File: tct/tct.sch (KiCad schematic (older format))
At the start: 6 parts, among them IC1 ATTINY85-P, P1 CONN_01X02, U1 DIL40_IC

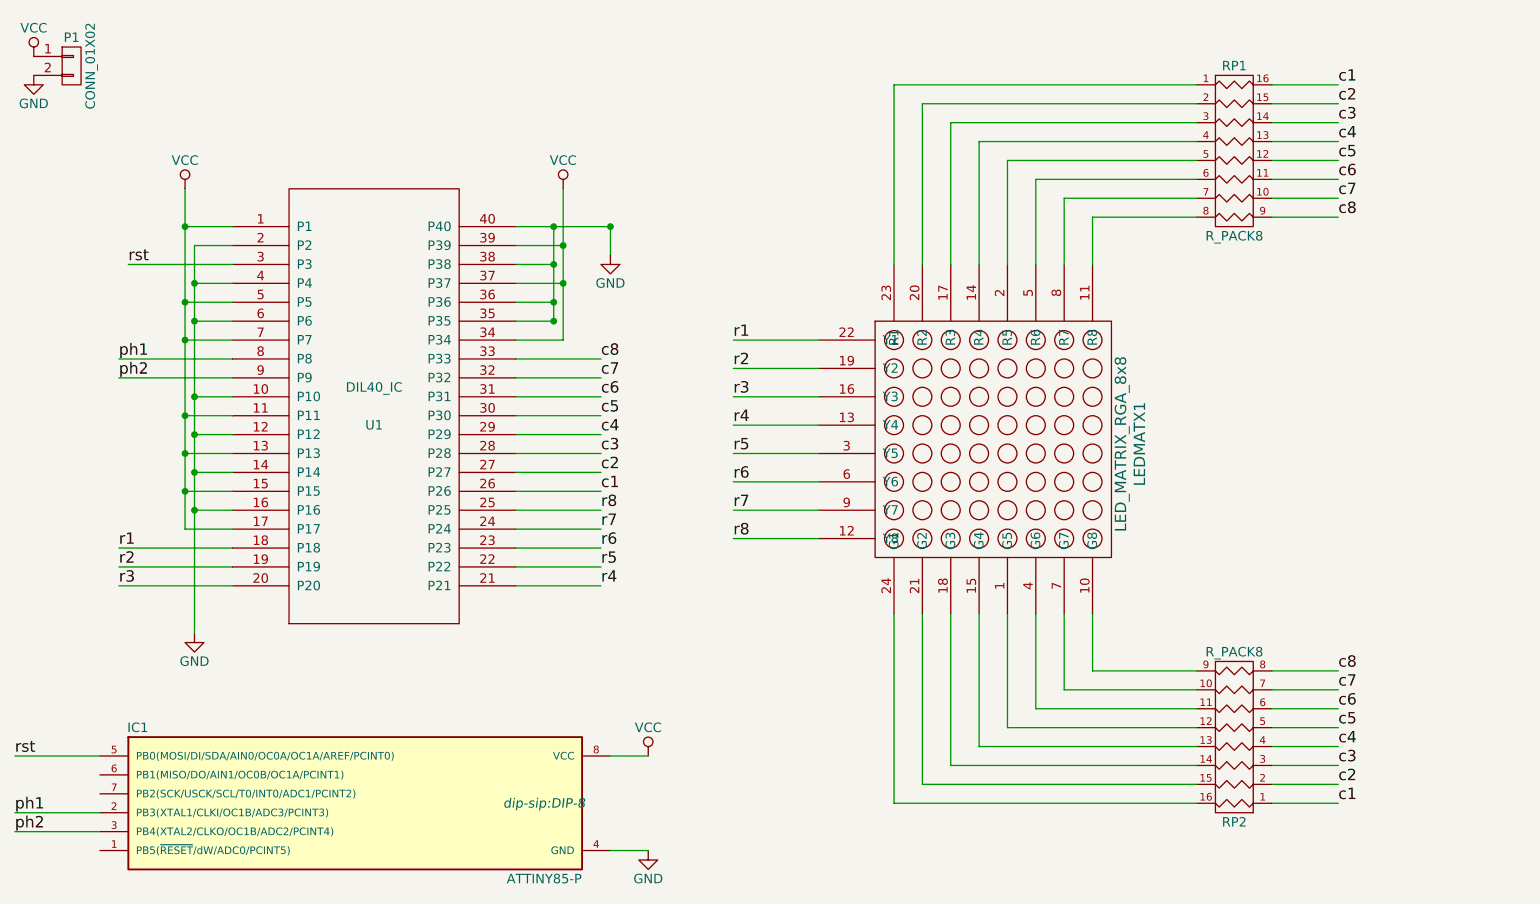
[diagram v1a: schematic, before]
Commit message: fixed layout with proper display pinout
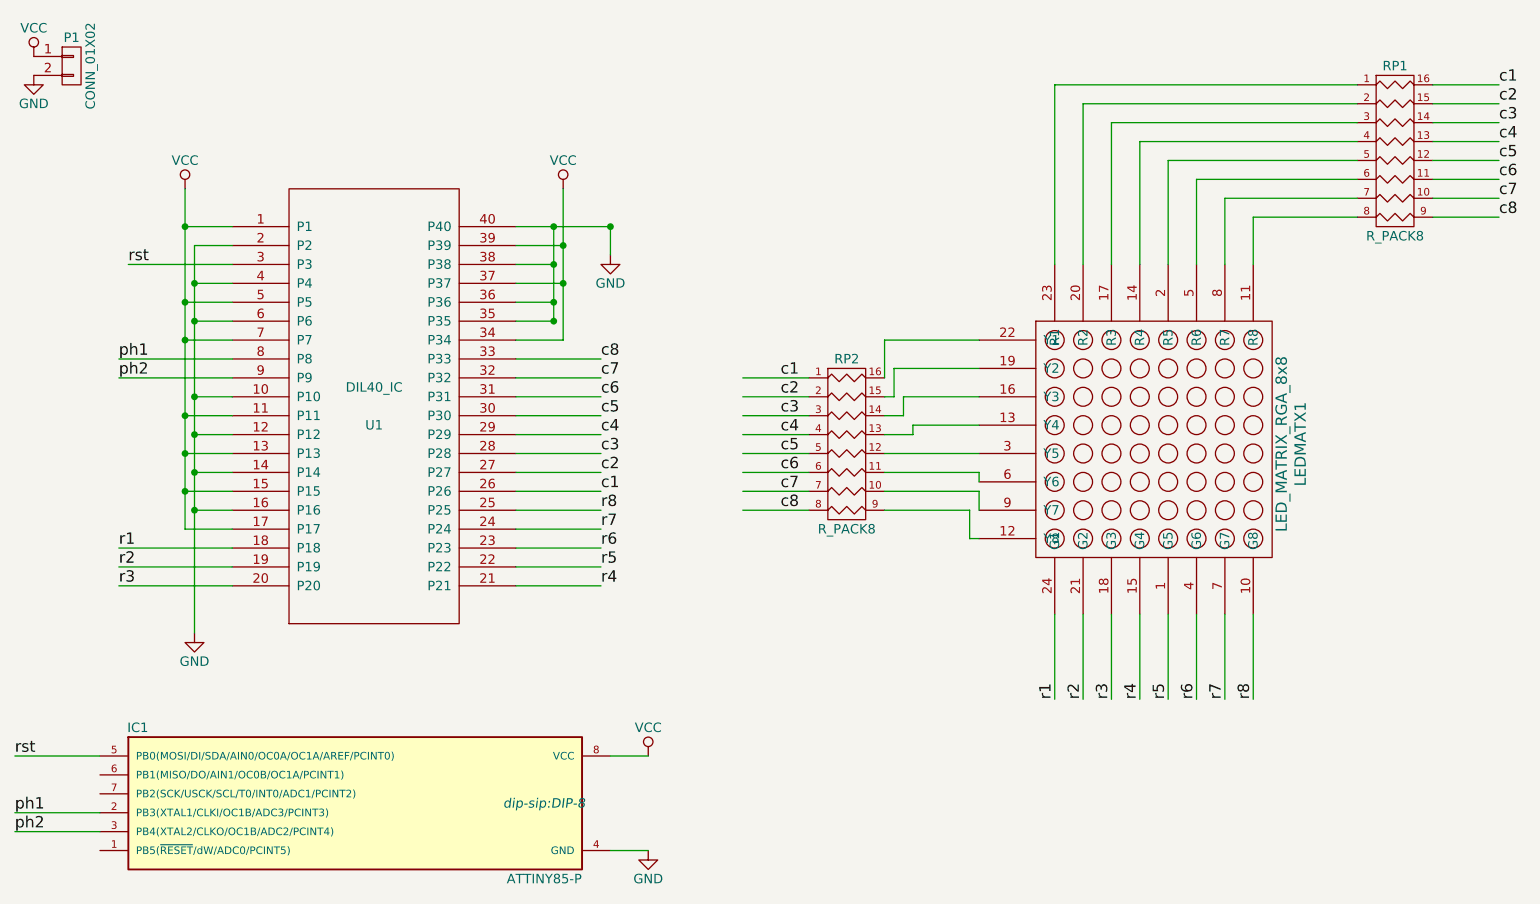
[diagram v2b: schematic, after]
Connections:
- wire segments 106 -> 109
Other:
- moved on the sheet: LEDMATX1, RP1, RP2
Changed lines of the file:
@@
 L LED_MATRIX_RGA_8x8 LEDMATX1
 U 1 1 58A54426
-P 8100 3350
-F 0 "LEDMATX1" V 8850 3350 60  0000 C CNN
-F 1 "LED_MATRIX_RGA_8x8" V 8750 3350 60  0000 C CNN
-F 2 "LED_MATRIX_RG_8x8:LED_MATRIX_RG_8x8" H 8100 3350 60  0001 C CNN
-F 3 "" H 8100 3350 60  0001 C CNN
-	1    8100 3350
+P 8950 3350
+F 0 "LEDMATX1" V 9700 3350 60  0000 C CNN
+F 1 "LED_MATRIX_RGA_8x8" V 9600 3350 60  0000 C CNN
+F 2 "LED_MATRIX_RG_8x8:LED_MATRIX_RG_8x8" H 8950 3350 60  0001 C CNN
+F 3 "" H 8950 3350 60  0001 C CNN
+	1    8950 3350
 	1    0    0    -1
 $EndComp
@@
 L R_PACK8 RP2
 U 1 1 58A5484C
-P 9350 4900
-F 0 "RP2" H 9350 5350 50  0000 C CNN
-F 1 "R_PACK8" H 9350 4450 50  0000 C CNN
-F 2 "Resistors_SMD:R_Array_Convex_8x0602" H 9350 4900 50  0001 C CNN
-F 3 "" H 9350 4900 50  0000 C CNN
-	1    9350 4900
-	-1   0    0    1
+P 7300 3350
+F 0 "RP2" H 7300 3800 50  0000 C CNN
+F 1 "R_PACK8" H 7300 2900 50  0000 C CNN
+F 2 "Resistors_SMD:R_Array_Convex_8x0602" H 7300 3350 50  0001 C CNN
+F 3 "" H 7300 3350 50  0000 C CNN
+	1    7300 3350
+	1    0    0    -1
 $EndComp
 $Comp
 L R_PACK8 RP1
 U 1 1 58A5487D
-P 9350 1800
-F 0 "RP1" H 9350 2250 50  0000 C CNN
-F 1 "R_PACK8" H 9350 1350 50  0000 C CNN
-F 2 "Resistors_SMD:R_Array_Convex_8x0602" H 9350 1800 50  0001 C CNN
-F 3 "" H 9350 1800 50  0000 C CNN
-	1    9350 1800
+P 10200 1800
+F 0 "RP1" H 10200 2250 50  0000 C CNN
+F 1 "R_PACK8" H 10200 1350 50  0000 C CNN
+F 2 "Resistors_SMD:R_Array_Convex_8x0602" H 10200 1800 50  0001 C CNN
+F 3 "" H 10200 1800 50  0000 C CNN
+	1    10200 1800
 	1    0    0    -1
 $EndComp
@@
 $EndComp
 Wire Wire Line
-	7550 5250 7550 4250
-Wire Wire Line
-	9150 5250 7550 5250
-Wire Wire Line
-	7700 5150 9150 5150
-Wire Wire Line
-	7700 4250 7700 5150
-Wire Wire Line
-	7850 5050 7850 4250
-Wire Wire Line
-	9150 5050 7850 5050
-Wire Wire Line
-	8000 4950 9150 4950
-Wire Wire Line
-	8000 4250 8000 4950
-Wire Wire Line
-	8150 4850 8150 4250
-Wire Wire Line
-	9150 4850 8150 4850
-Wire Wire Line
-	8300 4750 9150 4750
-Wire Wire Line
-	8300 4250 8300 4750
-Wire Wire Line
-	8450 4650 9150 4650
-Wire Wire Line
-	8450 4250 8450 4650
-Wire Wire Line
-	8600 4550 9150 4550
-Wire Wire Line
-	8600 4250 8600 4550
-Wire Wire Line
-	8600 2400 8600 2150
-Wire Wire Line
-	8600 2150 9150 2150
-Wire Wire Line
-	9150 2050 8450 2050
-Wire Wire Line
-	8450 2050 8450 2400
-Wire Wire Line
-	8300 2400 8300 1950
-Wire Wire Line
-	8300 1950 9150 1950
-Wire Wire Line
-	9150 1850 8150 1850
-Wire Wire Line
-	8150 1850 8150 2400
-Wire Wire Line
-	8000 2400 8000 1750
-Wire Wire Line
-	8000 1750 9150 1750
-Wire Wire Line
-	9150 1650 7850 1650
-Wire Wire Line
-	7850 1650 7850 2400
-Wire Wire Line
-	7700 2400 7700 1550
-Wire Wire Line
-	7700 1550 9150 1550
-Wire Wire Line
-	9150 1450 7550 1450
-Wire Wire Line
-	7550 1450 7550 2400
+	9450 2400 9450 2150
+Wire Wire Line
+	9450 2150 10000 2150
+Wire Wire Line
+	10000 2050 9300 2050
+Wire Wire Line
+	9300 2050 9300 2400
+Wire Wire Line
+	9150 2400 9150 1950
+Wire Wire Line
+	9150 1950 10000 1950
+Wire Wire Line
+	10000 1850 9000 1850
+Wire Wire Line
+	9000 1850 9000 2400
+Wire Wire Line
+	8850 2400 8850 1750
+Wire Wire Line
+	8850 1750 10000 1750
+Wire Wire Line
+	10000 1650 8700 1650
+Wire Wire Line
+	8700 1650 8700 2400
+Wire Wire Line
+	8550 2400 8550 1550
+Wire Wire Line
+	8550 1550 10000 1550
+Wire Wire Line
+	10000 1450 8400 1450
+Wire Wire Line
+	8400 1450 8400 2400
 Wire Wire Line
 	4050 2200 3800 2200
@@
 Connection ~ 3800 3400
 Wire Wire Line
-	5550 2500 5800 2500
+	5800 2500 5550 2500
 Wire Wire Line
 	5550 2300 5800 2300
@@
 Connection ~ 5750 2600
 Wire Wire Line
-	4050 3100 3850 3100
+	3850 3100 4050 3100
 Wire Wire Line
 	3850 2300 3850 4350
@@
 Connection ~ 5800 2500
 Wire Wire Line
-	5550 2700 5750 2700
+	5750 2700 5550 2700
 Connection ~ 5750 2700
 Wire Wire Line
@@
 	4050 4100 3450 4100
 Wire Wire Line
-	5750 2700 5750 2200
+	5750 2200 5750 2700
 Connection ~ 5750 2200
 Wire Wire Line
-	6050 2350 6050 2200
+	6050 2200 6050 2350
 Connection ~ 6050 2200
 Wire Wire Line
-	6050 2200 5550 2200
+	5550 2200 6050 2200
 Wire Wire Line
 	5550 4100 6000 4100
@@
 c8
 Wire Wire Line
-	9550 1450 9900 1450
-Wire Wire Line
-	9550 1550 9900 1550
-Wire Wire Line
-	9550 1650 9900 1650
-Wire Wire Line
-	9550 1750 9900 1750
-Wire Wire Line
-	9550 1850 9900 1850
-Wire Wire Line
-	9550 1950 9900 1950
-Wire Wire Line
-	9550 2050 9900 2050
-Wire Wire Line
-	9550 2150 9900 2150
-Wire Wire Line
-	9550 4550 9900 4550
-Wire Wire Line
-	9550 4650 9900 4650
-Wire Wire Line
-	9550 4750 9900 4750
-Wire Wire Line
-	9550 4850 9900 4850
-Wire Wire Line
-	9550 4950 9900 4950
-Wire Wire Line
-	9550 5050 9900 5050
-Wire Wire Line
-	9550 5150 9900 5150
-Wire Wire Line
-	9550 5250 9900 5250
-Wire Wire Line
-	7150 2800 6700 2800
-Wire Wire Line
-	7150 2950 6700 2950
-Wire Wire Line
-	7150 3100 6700 3100
-Wire Wire Line
-	7150 3250 6700 3250
-Wire Wire Line
-	7150 3400 6700 3400
-Wire Wire Line
-	7150 3550 6700 3550
-Wire Wire Line
-	7150 3700 6700 3700
-Wire Wire Line
-	7150 3850 6700 3850
-Text Label 6700 2800 0    60   ~ 0
+	10400 1450 10750 1450
+Wire Wire Line
+	10400 1550 10750 1550
+Wire Wire Line
+	10400 1650 10750 1650
+Wire Wire Line
+	10400 1750 10750 1750
+Wire Wire Line
+	10400 1850 10750 1850
+Wire Wire Line
+	10400 1950 10750 1950
+Wire Wire Line
+	10400 2050 10750 2050
+Wire Wire Line
+	10400 2150 10750 2150
+Wire Wire Line
+	6750 3000 7100 3000
+Wire Wire Line
+	6750 3100 7100 3100
+Wire Wire Line
+	6750 3200 7100 3200
+Wire Wire Line
+	6750 3300 7100 3300
+Wire Wire Line
+	6750 3400 7100 3400
+Wire Wire Line
+	6750 3500 7100 3500
+Wire Wire Line
+	6750 3600 7100 3600
+Wire Wire Line
+	6750 3700 7100 3700
+Wire Wire Line
+	8400 4250 8400 4700
+Wire Wire Line
+	8550 4250 8550 4700
+Wire Wire Line
+	8700 4250 8700 4700
+Wire Wire Line
+	8850 4250 8850 4700
+Wire Wire Line
+	9000 4250 9000 4700
+Wire Wire Line
+	9150 4250 9150 4700
+Wire Wire Line
+	9300 4250 9300 4700
+Wire Wire Line
+	9450 4250 9450 4700
+Text Label 8400 4700 1    60   ~ 0
 r1
-Text Label 6700 2950 0    60   ~ 0
+Text Label 8550 4700 1    60   ~ 0
 r2
-Text Label 6700 3100 0    60   ~ 0
+Text Label 8700 4700 1    60   ~ 0
 r3
-Text Label 6700 3250 0    60   ~ 0
+Text Label 8850 4700 1    60   ~ 0
 r4
-Text Label 6700 3400 0    60   ~ 0
+Text Label 9000 4700 1    60   ~ 0
 r5
-Text Label 6700 3550 0    60   ~ 0
+Text Label 9150 4700 1    60   ~ 0
 r6
-Text Label 6700 3700 0    60   ~ 0
+Text Label 9300 4700 1    60   ~ 0
 r7
-Text Label 6700 3850 0    60   ~ 0
+Text Label 9450 4700 1    60   ~ 0
 r8
 $Comp
@@
 	4050 2300 3850 2300
 Connection ~ 3850 2500
-Text Label 9900 1450 0    60   ~ 0
+Text Label 10750 1450 0    60   ~ 0
 c1
-Text Label 9900 1550 0    60   ~ 0
+Text Label 10750 1550 0    60   ~ 0
 c2
-Text Label 9900 1650 0    60   ~ 0
+Text Label 10750 1650 0    60   ~ 0
 c3
-Text Label 9900 1750 0    60   ~ 0
+Text Label 10750 1750 0    60   ~ 0
 c4
-Text Label 9900 1850 0    60   ~ 0
+Text Label 10750 1850 0    60   ~ 0
 c5
-Text Label 9900 1950 0    60   ~ 0
+Text Label 10750 1950 0    60   ~ 0
 c6
-Text Label 9900 2050 0    60   ~ 0
+Text Label 10750 2050 0    60   ~ 0
 c7
-Text Label 9900 2150 0    60   ~ 0
+Text Label 10750 2150 0    60   ~ 0
 c8
-Text Label 9900 4550 0    60   ~ 0
+Text Label 6950 3700 0    60   ~ 0
 c8
-Text Label 9900 4650 0    60   ~ 0
+Text Label 6950 3600 0    60   ~ 0
 c7
-Text Label 9900 4750 0    60   ~ 0
+Text Label 6950 3500 0    60   ~ 0
 c6
-Text Label 9900 4850 0    60   ~ 0
+Text Label 6950 3400 0    60   ~ 0
 c5
-Text Label 9900 4950 0    60   ~ 0
+Text Label 6950 3300 0    60   ~ 0
 c4
-Text Label 9900 5050 0    60   ~ 0
+Text Label 6950 3200 0    60   ~ 0
 c3
-Text Label 9900 5150 0    60   ~ 0
+Text Label 6950 3100 0    60   ~ 0
 c2
-Text Label 9900 5250 0    60   ~ 0
+Text Label 6950 3000 0    60   ~ 0
 c1
+Wire Wire Line
+	8000 2800 7500 2800
+Wire Wire Line
+	7500 2800 7500 3000
+Wire Wire Line
+	7500 3100 7550 3100
+Wire Wire Line
+	7550 3100 7550 2950
+Wire Wire Line
+	7550 2950 8000 2950
+Wire Wire Line
+	8000 3100 7600 3100
+Wire Wire Line
+	7600 3100 7600 3200
+Wire Wire Line
+	7600 3200 7500 3200
+Wire Wire Line
+	7500 3300 7650 3300
+Wire Wire Line
+	7650 3300 7650 3250
+Wire Wire Line
+	7650 3250 8000 3250
+Wire Wire Line
+	8000 3400 7500 3400
+Wire Wire Line
+	7500 3500 8000 3500
+Wire Wire Line
+	8000 3500 8000 3550
+Wire Wire Line
+	8000 3700 8000 3600
+Wire Wire Line
+	8000 3600 7500 3600
+Wire Wire Line
+	7500 3700 7950 3700
+Wire Wire Line
+	7950 3700 7950 3850
+Wire Wire Line
+	7950 3850 8000 3850
 $EndSCHEMATC
